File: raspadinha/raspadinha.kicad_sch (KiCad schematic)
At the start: 2 parts, among them J1 ATX-24

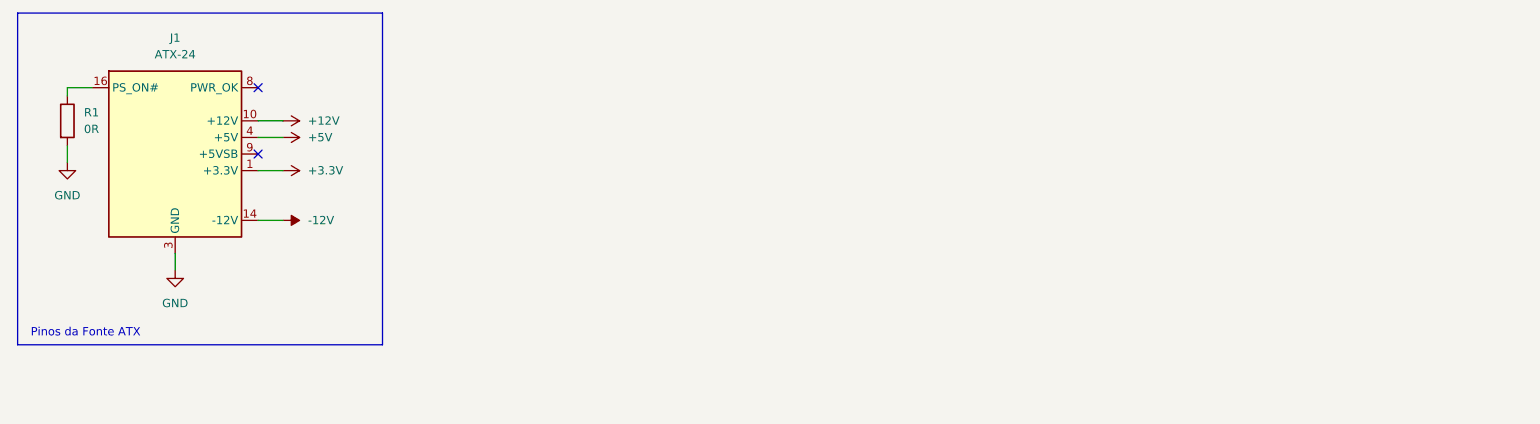
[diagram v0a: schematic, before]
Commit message: feat: Esquema elétrico do controle de temperatura
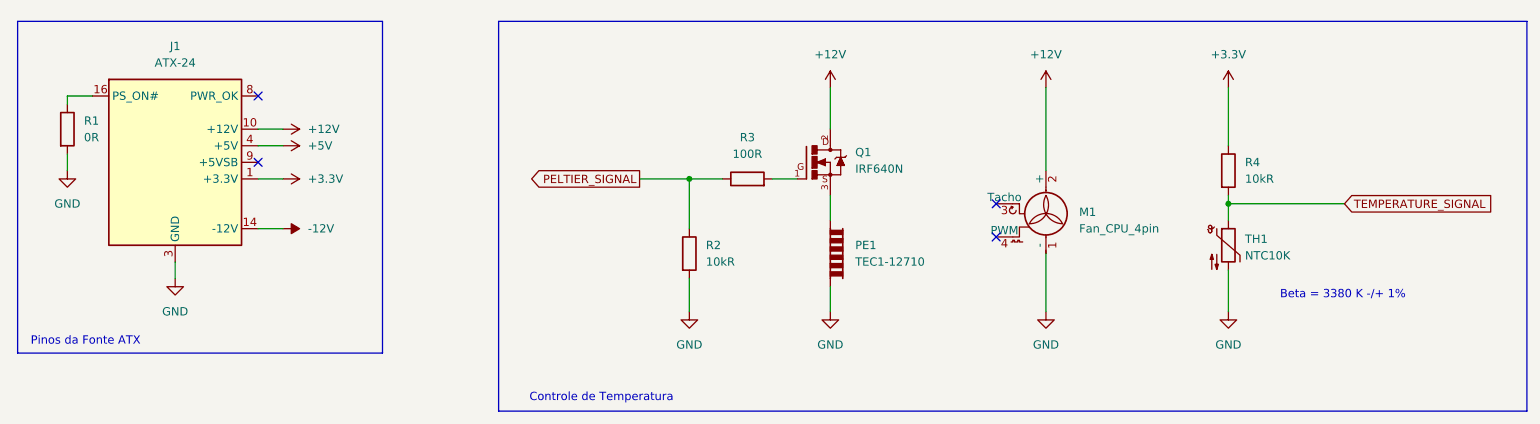
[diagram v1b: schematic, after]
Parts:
- added M1: Fan_CPU_4pin, symbol Motor:Fan_CPU_4pin
- added PE1: TEC1-12710, symbol Device:PeltierElement
- added Q1: IRF640N, symbol IRF640N:IRF640N
- added R2, R4: 10kR, symbol Device:R
- added R3: 100R, symbol Device:R
- added TH1: NTC10K, symbol Device:Thermistor_NTC
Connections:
- net +12V: now also M1.2 (+), Q1.2
- net +3.3V: now also R4.1
- net GND: now also M1.1 (-), PE1.2, R2.2, TH1.2
- new net: Q1.1, R3.2
- new net: PE1.1, Q1.3
- new net PELTIER_SIGNAL: R2.1, R3.1
- new net TEMPERATURE_SIGNAL: R4.2, TH1.1
- no-connect marks 2 -> 4
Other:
- note added: "Beta = 3380 K -/+ 1%"
- note added: "Controle de Temperatura"
- moved on the sheet: J1, R1
